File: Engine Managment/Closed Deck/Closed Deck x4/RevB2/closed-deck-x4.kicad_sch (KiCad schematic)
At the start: 0 parts

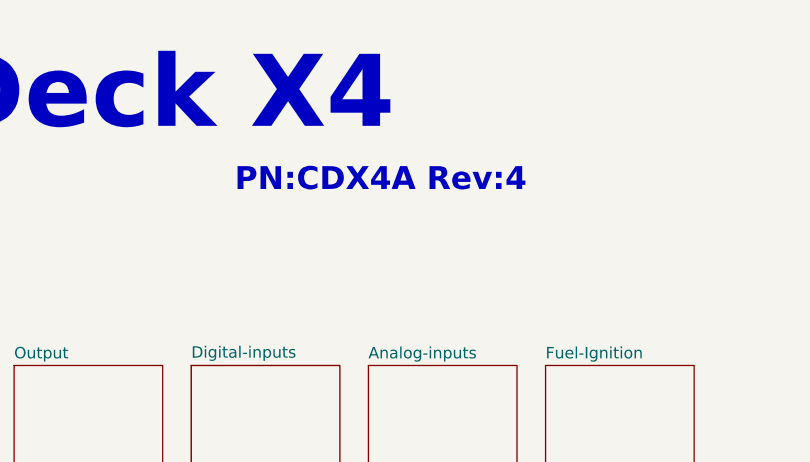
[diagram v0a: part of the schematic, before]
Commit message: INJ N-fet upload - Date corrections
N-Fet Initial Upload, recent upload date corrections.
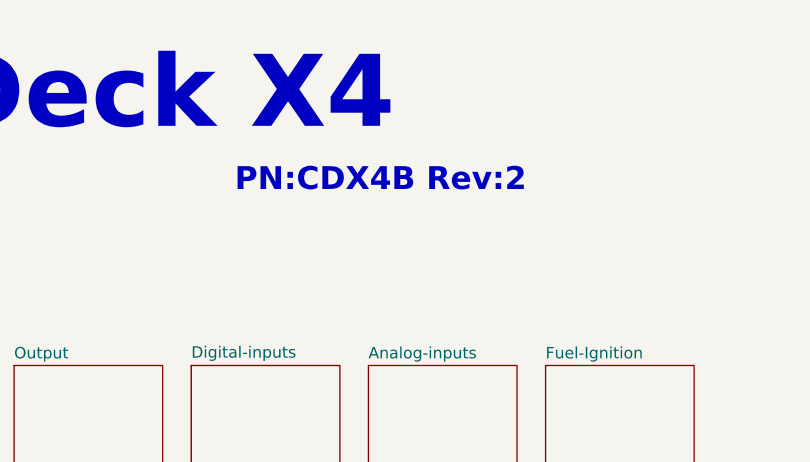
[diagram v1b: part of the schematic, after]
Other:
- note added: "PN:CDX4B Rev:2"
- note removed: "PN:CDX4A Rev:4"
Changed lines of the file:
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@@
 	(title_block
 		(title "Closed Deck X4")
-		(date "2026-01-03")
-		(rev "4")
+		(date "2026-05-06")
+		(rev "B2")
 		(company "OpenLogicEFI")
 		(comment 1 "openlogicefi.com")
@@
 		)
 	)
-	(text "PN:CDX4A Rev:4"
+	(text "PN:CDX4B Rev:2"
 		(exclude_from_sim no)
 		(at 169.926 82.55 0)
